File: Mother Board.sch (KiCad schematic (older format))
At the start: 102 parts, among them J1 Conn_01x02, J2 USB_B_Mini, J3 Conn_02x05_Odd_Even, J5 Conn_01x03, J6 Conn_01x03, SW1 SW_Push, U1 LM2595SX-3.3_NOPB, U2 LM2595SX-5.0_NOPB, U3 FT232RL, U4 STM32F407IGTx, U5 TPS2111APWR, Y1 Crystal_GND24

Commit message: Finished labeling card pins, changed rough layout
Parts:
- removed CARD0, CARD1, CARD2, CARD3, CARD4, CARD5, CARD6, CARD7: Conn_02x22_Odd_Even, connectors_mdg:5530843-4, symbol Connector_Generic:Conn_02x22_Odd_Even
- added CARD0, CARD1, CARD2, CARD3, CARD4, CARD5, CARD6, CARD7: Conn_02x22_Top_Bottom, connectors_mdg:5530843-4, symbol Connector_Generic:Conn_02x22_Top_Bottom
- added R41, R42, R43, R44, R45, R46, R47, R48: 10k, Resistor_SMD:R_0603_1608Metric_Pad1.05x0.95mm_HandSolder, symbol Device:R
- added U6: W25Q128JV-DTR, symbol flash_memory_mdg:W25Q128JV-DTR
- J1: footprint Connectors_Terminal_Blocks:TerminalBlock_bornier-2_P5.08mm -> TerminalBlock:TerminalBlock_bornier-2_P5.08mm
- U1, U2: footprint TO_SOT_Packages_SMD:TO-263-5_TabPin3 -> Package_TO_SOT_SMD:TO-263-5_TabPin3
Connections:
- net labels added: CARD0_GPIO0, CARD0_SENSE_NEG, CARD0_SENSE_POS, CARD0_TIM1_CH1N, CARD0_TIM3_CH1, CARD0_TIM9_CH1, CARD1_GPIO0, CARD1_SENSE_NEG, CARD1_SENSE_POS, CARD1_TIM1_CH2, CARD1_TIM1_CH2N, CARD1_TIM3_CH2, CARD1_TIM9_CH2, CARD2_GPIO0, CARD2_SENSE_NEG, CARD2_SENSE_POS, CARD2_TIM10_CH1, CARD2_TIM1_CH3, CARD2_TIM1_CH3N, CARD2_TIM3_CH3, CARD3_GPIO0, CARD3_GPIO3, CARD3_SENSE_NEG, CARD3_SENSE_POS, CARD3_TIM11_CH1, CARD3_TIM1_CH4, CARD3_TIM3_CH4, CARD4_GPIO0, CARD4_GPIO3, CARD4_SENSE_NEG, CARD4_SENSE_POS, CARD4_TIM12_CH1, CARD4_TIM4_CH1, CARD4_TIM5_CH1, CARD4_TIM8_CH1, CARD4_TIM8_CH1N, CARD5_GPIO0, CARD5_GPIO3, CARD5_SENSE_NEG, CARD5_SENSE_POS, CARD5_TIM12_CH2, CARD5_TIM4_CH2, CARD5_TIM5_CH2, CARD5_TIM8_CH2N, CARD6_GPIO0, CARD6_GPIO3, CARD6_SENSE_NEG, CARD6_SENSE_POS, CARD6_TIM13_CH1, CARD6_TIM4_CH3, CARD6_TIM5_CH3, CARD6_TIM8_CH3N, CARD7_GPIO0, CARD7_GPIO3, CARD7_GPIO6, CARD7_SENSE_NEG, CARD7_SENSE_POS, CARD7_TIM14_CH1, CARD7_TIM4_CH4, CARD7_TIM5_CH4, SPI2_MISO, SPI2_MOSI, SPI2_SCK, UART4_RX, UART4_TX, USART1_CTS, USART1_RTS, USART1_RX, USART1_TX, USART3_CTS, USART3_RTS, USART3_RX, USART3_TX, USART6_CTS, USART6_RTS, USART6_RX, USART6_TX
- net labels removed: CARD0_GPIO2, CARD0_GPIO4, CARD0_GPIO5, CARD0_TIM1_CH2, CARD0_TIM1_CH3, CARD0_TIM1_CH4, CARD1_GPIO2, CARD1_GPIO4, CARD1_GPIO5, CARD1_TIM8_CH1, CARD1_TIM8_CH2, CARD1_TIM8_CH3, CARD1_TIM8_CH4, CARD2_GPIO2, CARD2_GPIO4, CARD2_GPIO5, CARD2_TIM8_CH1, CARD2_TIM8_CH2, CARD2_TIM8_CH3, CARD2_TIM8_CH4, CARD3_GPIO5, CARD3_TIM8_CH1, CARD3_TIM8_CH2, CARD3_TIM8_CH3, CARD3_TIM8_CH4, CARD4_TIM1_CH1, CARD4_TIM1_CH2, CARD4_TIM1_CH3, CARD4_TIM1_CH4, CARD4_TIM3_CH1, CARD5_TIM3_CH2, CARD5_TIM8_CH1, CARD5_TIM8_CH3, CARD5_TIM8_CH4, CARD6_TIM3_CH3, CARD6_TIM8_CH1, CARD6_TIM8_CH2, CARD6_TIM8_CH4, CARD7_TIM3_CH4, CARD7_TIM8_CH1, CARD7_TIM8_CH2, CARD7_TIM8_CH3, UART5_RX_PD2, UART5_TX_PC12, USART1_CTS_PA11, USART1_RTS_PA12, USART1_RX_PB7, USART1_TX_PB6, USART3_CTS_PB13, USART3_CTS_PD11, USART3_RTS_PB14, USART3_RTS_PD12, USART3_RX_PB11, USART3_RX_PD9, USART3_TX_PB10, USART3_TX_PD8
- wire segments 210 -> 218

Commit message: Moved power supply to external board.  Reworked rough layout
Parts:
- removed D1, D2: D_Schottky, digikey-footprints:DO-214AB, symbol Device:D_Schottky
- removed J1: Conn_01x02, TerminalBlock:TerminalBlock_bornier-2_P5.08mm, symbol Connector_Generic:Conn_01x02
- removed L1, L2: L, my_inductors:Wurth_SMD_Inductor_7447709101, symbol Device:L
- removed R10: 10K, Resistor_SMD:R_0603_1608Metric_Pad1.05x0.95mm_HandSolder, symbol Device:R
- removed R11: 265R, Resistor_SMD:R_0603_1608Metric_Pad1.05x0.95mm_HandSolder, symbol Device:R
- removed R12: 400R, Resistor_SMD:R_0603_1608Metric_Pad1.05x0.95mm_HandSolder, symbol Device:R
- removed U1: LM2595SX-3.3_NOPB, Package_TO_SOT_SMD:TO-263-5_TabPin3, symbol Mother-Board-rescue:LM2595SX-3.3_NOPB-Voltage_Regulators
- removed U2: LM2595SX-5.0_NOPB, Package_TO_SOT_SMD:TO-263-5_TabPin3, symbol Mother-Board-rescue:LM2595SX-5.0_NOPB-Voltage_Regulators
- added J1, J4, J7: Conn_01x04, TerminalBlock:TerminalBlock_bornier-4_P5.08mm, symbol Connector_Generic:Conn_01x04
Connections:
- wire segments 218 -> 191
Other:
- moved on the sheet: C1, C17, C2

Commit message: last commit before shifting to prototype version
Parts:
- added C?: CP, Capacitor_THT:CP_Radial_D8.0mm_P3.50mm, symbol Device:CP
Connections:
- net labels removed: SPI1_MISO, SPI1_MOSI, SPI1_SCK
- wire segments 191 -> 200
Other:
- moved on the sheet: C1, C17, C2, C3, C4, D3, D4, R1, R2

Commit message: worked on layout for power mux section
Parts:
- removed C18: 0.1uF, Capacitor_SMD:C_0603_1608Metric_Pad1.05x0.95mm_HandSolder, symbol Device:C
- removed CARD2, CARD3, CARD5, CARD6, CARD7: Conn_02x22_Top_Bottom, connectors_mdg:5530843-4, symbol Connector_Generic:Conn_02x22_Top_Bottom
- removed R44, R45, R46, R47, R48: 10k, Resistor_SMD:R_0603_1608Metric_Pad1.05x0.95mm_HandSolder, symbol Device:R
- removed U4: STM32F407IGTx, Package_QFP:LQFP-176_24x24mm_P0.5mm, symbol MCU_ST_STM32F4:STM32F407IGTx
- removed U5: TPS2111APWR, Package_SO:TSSOP-8_4.4x3mm_P0.65mm, symbol Power_Management_MDG:TPS2111APWR
- added C27, C28: 0.1uF, Capacitor_SMD:C_0603_1608Metric_Pad1.05x0.95mm_HandSolder, symbol Device:C
- added D1, D2: LED, LED_SMD:LED_1206_3216Metric_Pad1.42x1.75mm_HandSolder, symbol Device:LED
- added L1: L, Inductor_SMD:L_1206_3216Metric, symbol Device:L
- added R10, R11: 0R, Resistor_SMD:R_0603_1608Metric_Pad1.05x0.95mm_HandSolder, symbol Device:R
- added R12: 23.7K, Resistor_SMD:R_0603_1608Metric_Pad1.05x0.95mm_HandSolder, symbol Device:R
- added U1: SC189, Package_TO_SOT_SMD:SOT-23-5_HandSoldering, symbol voltage_regulators_mdg:SC189
- added U2, U4: TPS2121, packages_mdg:Texas_VQFN_HR_12, symbol Power_Management_MDG:TPS2121
- added U5: STM32F407VGTx, Package_QFP:LQFP-100_14x14mm_P0.5mm, symbol MCU_ST_STM32F4:STM32F407VGTx
- C19: value 0.1uF -> 10uF
- C21: value 0.1uF -> 22uF
- C22, C23: value 0.1uF -> 1uF
- C24, C25: value 0.1uF -> 2.2uF
- C9: value 0.1uF -> 4.7uF
- R1, R2: value R -> 330R
- R19, R21, R23, R32, R34: value 10k -> 5K
- R20, R24: value 10k -> 13.7K
- R22: value 10k -> 23.7K
- R33: value 10k -> 10.2K
- R35, R36: value 10k -> 10K
- R37, R38: value 10k -> 330R
- R39, R40: value 10k -> 20K
- U6: footprint (none) -> Package_SO:SOIC-8_3.9x4.9mm_P1.27mm
- Y1: footprint Crystals:Crystal_SMD_SeikoEpson_TSX3225-4pin_3.2x2.5mm -> Crystal:Crystal_SMD_SeikoEpson_TSX3225-4Pin_3.2x2.5mm_HandSoldering
- gave numbers to parts that had none: 1
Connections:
- net labels added: 3V3_EXT, 3v3_REG_EN, 3v3_REG_OUT, 5V_EXT, CARD4_TIM12_CH2, I2C1_SCL, I2C1_SDA, RX_LED, SPI3_MISO, SPI3_MOSI, SPI3_SCK, SPI_FLASH_CS, TX_LED, USART2_CTS, USART2_RTS, USART2_RX, USART2_TX, USB_D+, USB_D-, USB_VBUS
- net labels removed: CARD2_ADD0, CARD2_ADD1, CARD2_ADD2, CARD2_CS, CARD2_ENABLE, CARD2_GPIO0, CARD2_GPIO1, CARD2_SENSE_NEG, CARD2_SENSE_POS, CARD2_STATUS, CARD2_TIM10_CH1, CARD2_TIM1_CH3, CARD2_TIM1_CH3N, CARD2_TIM2_CH3, CARD2_TIM3_CH3, CARD3_ADD0, CARD3_ADD1, CARD3_ADD2, CARD3_CS, CARD3_ENABLE, CARD3_GPIO0, CARD3_GPIO1, CARD3_GPIO2, CARD3_GPIO3, CARD3_GPIO4, CARD3_SENSE_NEG, CARD3_SENSE_POS, CARD3_STATUS, CARD3_TIM11_CH1, CARD3_TIM1_CH4, CARD3_TIM2_CH4, CARD3_TIM3_CH4, CARD4_TIM12_CH1, CARD5_ADD0, CARD5_ADD1, CARD5_ADD2, CARD5_CS, CARD5_ENABLE, CARD5_GPIO0, CARD5_GPIO1, CARD5_GPIO2, CARD5_GPIO3, CARD5_GPIO4, CARD5_GPIO5, CARD5_SENSE_NEG, CARD5_SENSE_POS, CARD5_STATUS, CARD5_TIM12_CH2, CARD5_TIM4_CH2, CARD5_TIM5_CH2, CARD5_TIM8_CH2, CARD5_TIM8_CH2N, CARD6_ADD0, CARD6_ADD1, CARD6_ADD2, CARD6_CS, CARD6_ENABLE, CARD6_GPIO0, CARD6_GPIO1, CARD6_GPIO2, CARD6_GPIO3, CARD6_GPIO4, CARD6_GPIO5, CARD6_SENSE_NEG, CARD6_SENSE_POS, CARD6_STATUS, CARD6_TIM13_CH1, CARD6_TIM4_CH3, CARD6_TIM5_CH3, CARD6_TIM8_CH3, CARD6_TIM8_CH3N, CARD7_ADD0, CARD7_ADD1, CARD7_ADD2, CARD7_CS, CARD7_ENABLE, CARD7_GPIO0, CARD7_GPIO1, CARD7_GPIO2, CARD7_GPIO3, CARD7_GPIO4, CARD7_GPIO5, CARD7_GPIO6, CARD7_SENSE_NEG, CARD7_SENSE_POS, CARD7_STATUS, CARD7_TIM14_CH1, CARD7_TIM4_CH4, CARD7_TIM5_CH4, CARD7_TIM8_CH4, SPI2_MISO, SPI2_MISO_PI2, SPI2_MOSI, SPI2_MOSI_PI3, SPI2_SCK, SPI2_SCK_PI1, UART4_RX, UART4_TX, USART2_CTS_PD3, USART2_RTS_PD4, USART2_RX_PD6, USART2_TX_PD5, USART6_CTS, USART6_RTS, USART6_RX, USART6_TX
- wire segments 200 -> 184
- no-connect marks 2 -> 11
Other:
- moved on the sheet: C1, C11, C12, C13, C14, C15, C16, C17, C18, C2, C3, C4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

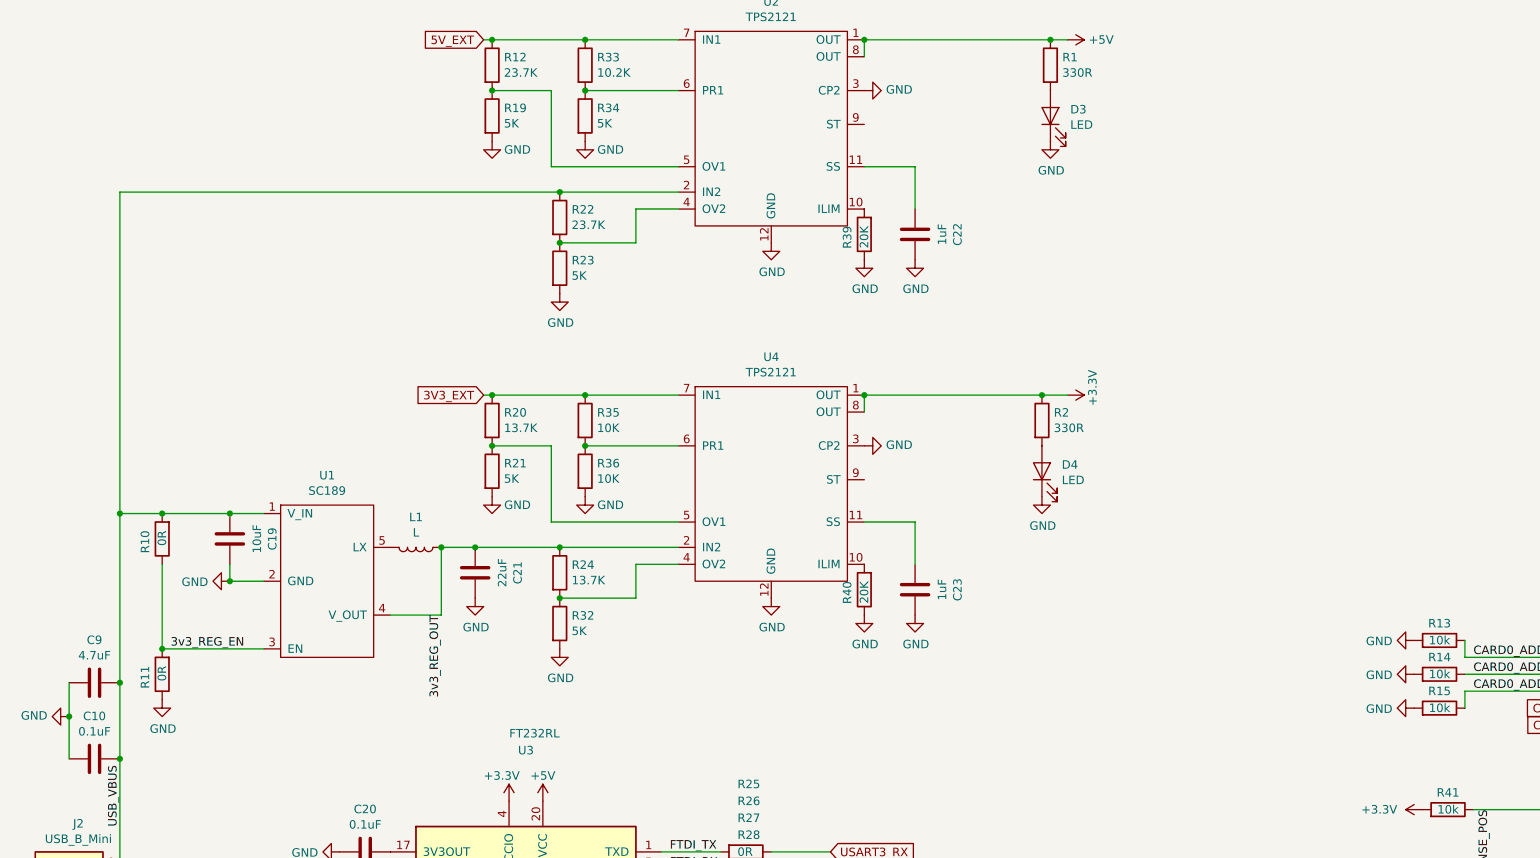
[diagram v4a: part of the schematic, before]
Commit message: worked on layout of power mux, added inverter to enable 3v3 regulator
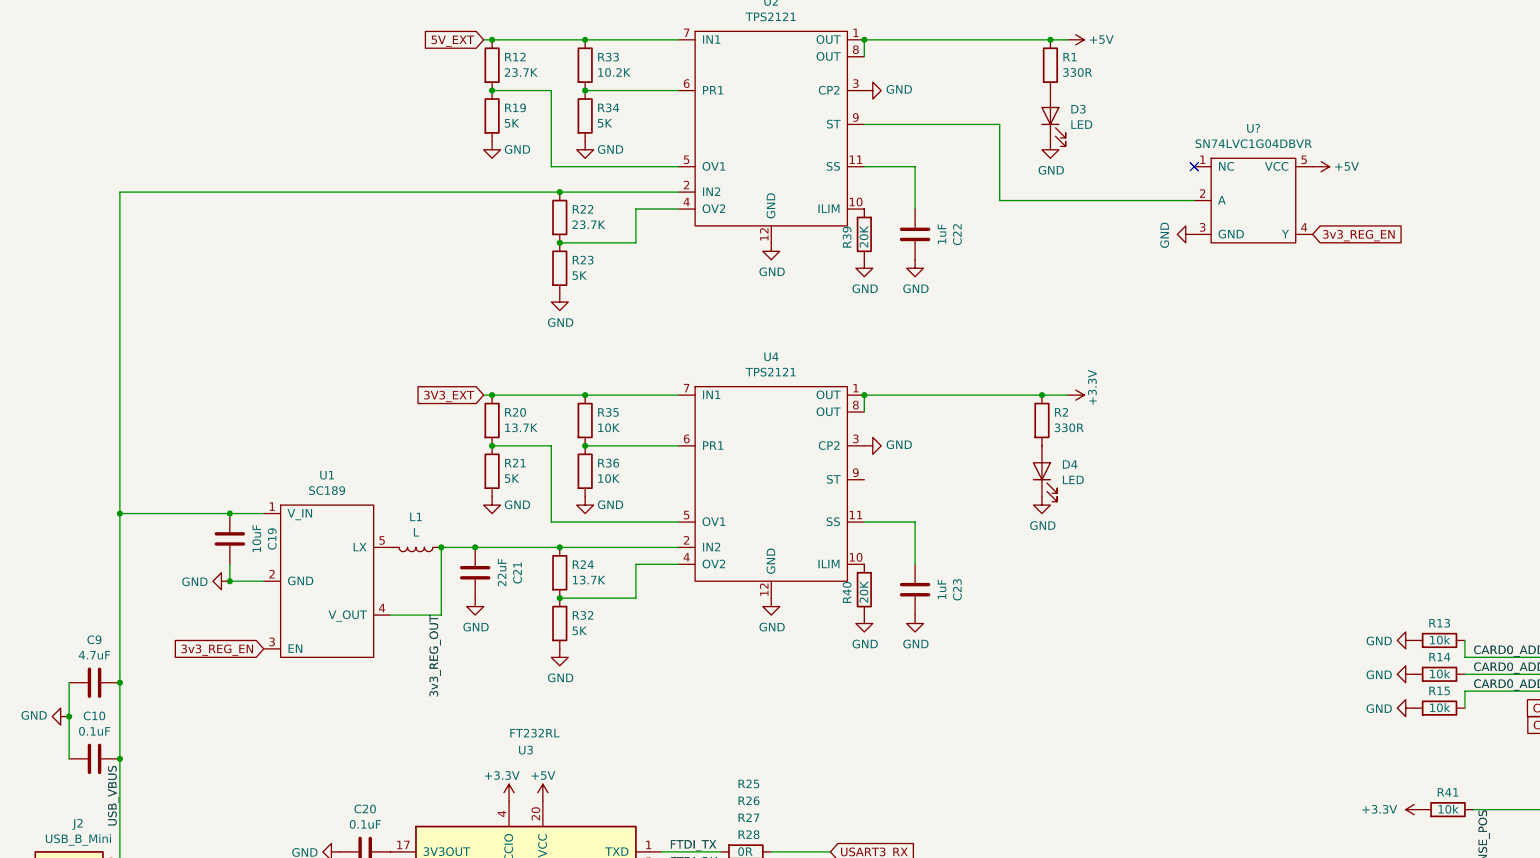
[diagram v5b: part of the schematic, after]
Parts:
- removed R10, R11: 0R, Resistor_SMD:R_0603_1608Metric_Pad1.05x0.95mm_HandSolder, symbol Device:R
- added U?: SN74LVC1G04DBVR, Package_TO_SOT_SMD:SOT-23-5_HandSoldering, symbol logic_mdg:SN74LVC1G04DBVR
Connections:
- net +5V: now also U?.5 (VCC)
- net 3v3_REG_EN: now also U?.4 (Y)
- net GND: now also U?.3 (GND)
- net at U2.9 (ST): now also U?.2 (A)
- no-connect marks 11 -> 12
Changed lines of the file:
@@
 	1    0    0    -1
 $EndComp
-Wire Wire Line
-	1800 11200 2050 11200
 $Comp
 L Device:C C19
@@
 Connection ~ 2450 11600
 $Comp
-L Device:R R10
-U 1 1 5DC00C33
-P 2050 11350
-F 0 "R10" V 2150 11300 50  0000 L CNN
-F 1 "0R" V 2050 11300 50  0000 L CNN
-F 2 "Resistor_SMD:R_0603_1608Metric_Pad1.05x0.95mm_HandSolder" V 1980 11350 50  0001 C CNN
-F 3 "~" H 2050 11350 50  0001 C CNN
-	1    2050 11350
-	-1   0    0    1
-$EndComp
-Connection ~ 2050 11200
-Wire Wire Line
-	2050 11200 2450 11200
-Wire Wire Line
-	2050 11500 2050 12000
-$Comp
-L Device:R R11
-U 1 1 5DC06C2C
-P 2050 12150
-F 0 "R11" V 2150 12100 50  0000 L CNN
-F 1 "0R" V 2050 12100 50  0000 L CNN
-F 2 "Resistor_SMD:R_0603_1608Metric_Pad1.05x0.95mm_HandSolder" V 1980 12150 50  0001 C CNN
-F 3 "~" H 2050 12150 50  0001 C CNN
-	1    2050 12150
-	-1   0    0    1
-$EndComp
-$Comp
-L power:GND #PWR0191
-U 1 1 5DC075DE
-P 2050 12300
-F 0 "#PWR0191" H 2050 12050 50  0001 C CNN
-F 1 "GND" H 2055 12127 50  0000 C CNN
-F 2 "" H 2050 12300 50  0001 C CNN
-F 3 "" H 2050 12300 50  0001 C CNN
-	1    2050 12300
-	1    0    0    -1
-$EndComp
-$Comp
 L Device:L L1
 U 1 1 5DC08DBD
@@
 Wire Wire Line
 	1800 12650 1800 13300
-Connection ~ 2050 12000
-Wire Wire Line
-	2050 12000 2650 12000
 Connection ~ 7250 10500
 Wire Wire Line
@@
 Text Label 3700 11800 3    50   ~ 0
 3v3_REG_OUT
-Text Label 2100 12000 0    50   ~ 0
+$Comp
+L logic_mdg:SN74LVC1G04DBVR U?
+U 1 1 5D954C10
+P 8500 9350
+F 0 "U?" H 8500 9775 50  0000 C CNN
+F 1 "SN74LVC1G04DBVR" H 8500 9684 50  0000 C CNN
+F 2 "Package_TO_SOT_SMD:SOT-23-5_HandSoldering" H 8500 9350 50  0001 C CNN
+F 3 "" H 8500 9350 50  0001 C CNN
+	1    8500 9350
+	1    0    0    -1
+$EndComp
+Wire Wire Line
+	1800 11200 2450 11200
+Text GLabel 2650 12000 0    50   Input ~ 0
 3v3_REG_EN
+Text GLabel 8850 9550 2    50   Input ~ 0
+3v3_REG_EN
+Wire Wire Line
+	6200 8900 7000 8900
+Wire Wire Line
+	7000 8900 7000 9350
+Wire Wire Line
+	7000 9350 8150 9350
+NoConn ~ 8150 9150
+$Comp
+L power:GND #PWR?
+U 1 1 5D9826F2
+P 8150 9550
+F 0 "#PWR?" H 8150 9300 50  0001 C CNN
+F 1 "GND" H 8155 9377 50  0000 C CNN
+F 2 "" H 8150 9550 50  0001 C CNN
+F 3 "" H 8150 9550 50  0001 C CNN
+	1    8150 9550
+	0    1    1    0
+$EndComp
+$Comp
+L power:+5V #PWR?
+U 1 1 5D9849F2
+P 8850 9150
+F 0 "#PWR?" H 8850 9000 50  0001 C CNN
+F 1 "+5V" V 8850 9350 50  0000 C CNN
+F 2 "" H 8850 9150 50  0001 C CNN
+F 3 "" H 8850 9150 50  0001 C CNN
+	1    8850 9150
+	0    1    1    0
+$EndComp
 $EndSCHEMATC

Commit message: all tracks connected, need to clean up layout before ordering.
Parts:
- removed C1, C17, C18, C2, C3, C4: CP, Capacitor_THT:CP_Radial_D8.0mm_P3.50mm, symbol Device:CP
- GND1: renamed from TP6; footprint Measurement_Points:Test_Point_Keystone_5010-5014_Multipurpose -> test_points_mdg:Keystone_5010
- GND2: renamed from TP7; footprint Measurement_Points:Test_Point_Keystone_5010-5014_Multipurpose -> test_points_mdg:Keystone_5010
- GND3: renamed from TP8; footprint Measurement_Points:Test_Point_Keystone_5010-5014_Multipurpose -> test_points_mdg:Keystone_5010
- GND4: renamed from TP9; footprint Measurement_Points:Test_Point_Keystone_5010-5014_Multipurpose -> test_points_mdg:Keystone_5010
- GND5: renamed from TP10; footprint Measurement_Points:Test_Point_Keystone_5010-5014_Multipurpose -> test_points_mdg:Keystone_5010
- I2C1_SCL1: renamed from TP1; footprint Measurement_Points:Test_Point_Keystone_5010-5014_Multipurpose -> test_points_mdg:Keystone_5010
- I2C1_SDA1: renamed from TP2; footprint Measurement_Points:Test_Point_Keystone_5010-5014_Multipurpose -> test_points_mdg:Keystone_5010
- SPI3_MISO1: renamed from TP4; footprint Measurement_Points:Test_Point_Keystone_5010-5014_Multipurpose -> test_points_mdg:Keystone_5010
- SPI3_MOSI1: renamed from TP5; footprint Measurement_Points:Test_Point_Keystone_5010-5014_Multipurpose -> test_points_mdg:Keystone_5010
- SPI3_SCK1: renamed from TP3; footprint Measurement_Points:Test_Point_Keystone_5010-5014_Multipurpose -> test_points_mdg:Keystone_5010
- gave numbers to parts that had none: 1
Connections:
- net IC1_SCL is gone; now on net I2C1_SCL: I2C1_SCL1.1
- net IC1_SDA is gone; now on net I2C1_SDA: I2C1_SDA1.1
- net +5V: now also C10.2, C9.2
- net CARD0_TIM1_CH1: now also U5.42 (PE11); no longer U5.40 (PE9)
- net CARD0_TIM1_CH1N: now also U5.41 (PE10); no longer U5.39 (PE8)
- net CARD0_TIM3_CH1: now also U5.32 (PA7); no longer U5.31 (PA6)
- net CARD1_TIM1_CH2: now also U5.40 (PE9); no longer U5.42 (PE11)
- net CARD1_TIM1_CH2N: now also U5.39 (PE8); no longer U5.41 (PE10)
- net CARD1_TIM3_CH2: now also U5.31 (PA6); no longer U5.32 (PA7)
- net SPI_FLASH_CS: now also U5.43 (PE12)
- net USB_VBUS: no longer C10.2, C9.2
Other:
- moved on the sheet: C10, C9

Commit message: Needs final clean up, then ready for ordering
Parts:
- added 3v3_MUX_ST1, 5V_MUX_ST1: TestPoint, TestPoint:TestPoint_Pad_D1.0mm, symbol Connector:TestPoint
- added D10, D11, D5, D6, D7, D8, D9: LED, LED_SMD:LED_1206_3216Metric_Pad1.42x1.75mm_HandSolder, symbol Device:LED
- added Q1, Q2, Q3, Q4, Q5, Q6, Q7: Q_NMOS_GSD, Package_TO_SOT_SMD:SOT-323_SC-70_Handsoldering, symbol Device:Q_NMOS_GSD
- added R10, R44, R45, R48, R49, R52, R53: 10k, Resistor_SMD:R_0603_1608Metric_Pad1.05x0.95mm_HandSolder, symbol Device:R
- added R11, R46, R47, R50, R51, R54, R55: 330R, Resistor_SMD:R_0603_1608Metric_Pad1.05x0.95mm_HandSolder, symbol Device:R
- added SPI_FLASH_CS1, USART3_CTS1, USART3_RTS1, USART3_RX1, USART3_TX1: TestPoint, test_points_mdg:TestPoint_Keystone_5015_Micro-Minature, symbol Connector:TestPoint
- GND1, GND2, GND3, GND4, GND5, I2C1_SCL1, I2C1_SDA1, SPI3_MISO1, SPI3_MOSI1, SPI3_SCK1: footprint test_points_mdg:Keystone_5010 -> test_points_mdg:TestPoint_Keystone_5015_Micro-Minature
- J1: Part Number 1 (none) -> 796638-4; Part Number 2 (none) -> 796634-4
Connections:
- net +3V3: now also D10.2 (A), D11.2 (A), D5.2 (A), D6.2 (A), D7.2 (A), D8.2 (A), D9.2 (A)
- net CARD0_ENABLE: now also Q3.1 (G), R45.1
- net CARD0_STATUS: now also Q2.1 (G), R44.1
- net CARD1_ENABLE: now also Q5.1 (G), R49.1
- net CARD1_STATUS: now also Q4.1 (G), R48.1
- net CARD4_ENABLE: now also Q7.1 (G), R53.1
- net CARD4_STATUS: now also Q6.1 (G), R52.1
- net GND: now also Q1.2 (S), Q2.2 (S), Q3.2 (S), Q4.2 (S), Q5.2 (S), Q6.2 (S), Q7.2 (S), R10.2, R44.2, R45.2, R48.2, R49.2, R52.2, R53.2
- net SPI_FLASH_CS: now also SPI_FLASH_CS1.1
- net USART3_CTS: now also USART3_CTS1.1
- net USART3_RTS: now also USART3_RTS1.1
- net USART3_RX: now also USART3_RX1.1
- net USART3_TX: now also USART3_TX1.1
- net MICRO_STATUS: now reaches U5.33 (PC4)
- net MICRO_STATUS: now also Q1.1 (G), R10.1
- net at U2.9 (ST), U7.2 (A): now also 5V_MUX_ST1.1
- net at U4.9 (ST): now also 3v3_MUX_ST1.1
- new net: Q2.3 (D), R46.2
- new net: D6.1 (K), R46.1
- new net: Q4.3 (D), R50.2
- new net: D8.1 (K), R50.1
- new net: Q6.3 (D), R54.2
- new net: D10.1 (K), R54.1
- new net: Q3.3 (D), R47.2
- new net: D7.1 (K), R47.1
- new net: Q5.3 (D), R51.2
- new net: D9.1 (K), R51.1
- new net: Q7.3 (D), R55.2
- new net: D11.1 (K), R55.1
- new net: Q1.3 (D), R11.2
- new net: D5.1 (K), R11.1
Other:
- moved on the sheet: GND1, GND2, GND3, GND4, GND5, I2C1_SCL1, I2C1_SDA1, J3, SPI3_MISO1, SPI3_MOSI1, SPI3_SCK1, U6

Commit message: added part numbers to schematic, pcb ordered
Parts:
- added GND6: TestPoint, test_points_mdg:TestPoint_Keystone_5015_Micro-Minature, symbol Connector:TestPoint
- added R56, R57, R58, R59, R60: 10k, Resistor_SMD:R_0603_1608Metric_Pad1.05x0.95mm_HandSolder, symbol Device:R
- D10, D11, D3, D4, D5, D6, D7, D8, D9: Part Number (none) -> RED LED 1206
- GND1, GND2, GND3, GND4, GND5, I2C1_SCL1, I2C1_SDA1, SPI3_MISO1, SPI3_MOSI1, SPI3_SCK1, SPI_FLASH_CS1, USART3_CTS1, USART3_RTS1, USART3_RX1, USART3_TX1: Part Number (none) -> 5015
- J1: Part Number (none) -> 796638-4; Part Number 1 796638-4 -> (none)
- J3: Part Number (none) -> FTSH-105-01-F-D-K
- J4, J7: Part Number (none) -> 796638-4
- L1: value L -> 1 uH; Part Number (none) -> CIGW252010GL1R0MNE
- Q1, Q2, Q3, Q4, Q5, Q6, Q7: Part Number (none) -> 2N7002BKVL
- SW1: Part Number (none) -> FSM2JMTR
- U1: Part Number (none) -> SC189
- U2, U4: Part Number (none) -> TPS2121
- U3: Part Number (none) -> FT232RL
- U5: Part Number (none) -> STM32F407VGT6
- U6: Part Number (none) -> W25Q128JVSIQ
- U7: Part Number (none) -> SN74LVC1G04DBVR
- Y1: Part Number (none) -> TSX-3225 26.0000MF09Z-AC3
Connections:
- net +3V3: now also R56.1, R57.1, R58.1, R59.1, R60.1
- net CARD0_CS: now also R56.2
- net CARD1_CS: now also R58.2
- net CARD4_CS: now also R57.2
- net GND: now also GND6.1
- net SPI3_MISO: now also R60.2
- net SPI_FLASH_CS: now also R59.2
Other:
- moved on the sheet: J1, J4, J7
